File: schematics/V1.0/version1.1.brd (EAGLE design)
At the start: 66 x 45 mm, 89 parts, among them IC1 ADG1604S, IC2 LM317MBSTT3, IC3 AD8610MR, IC4 AD8610MR, IC5 337IMP, Q1 16MHz, T1 BC847, T2 BC847, T3 BC847, T4 BC847, X2 BU-SMA-H

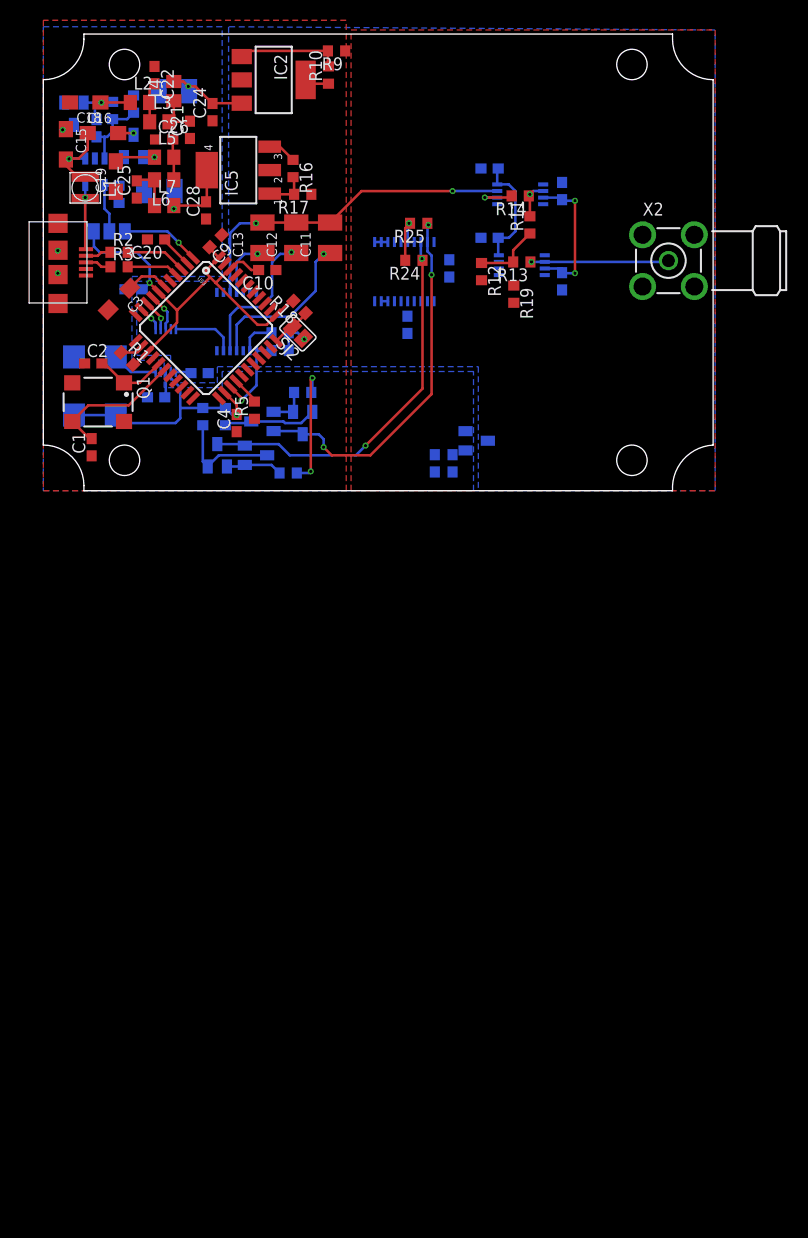
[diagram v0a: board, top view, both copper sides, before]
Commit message: change the circuit diagramm because of amplification-issues
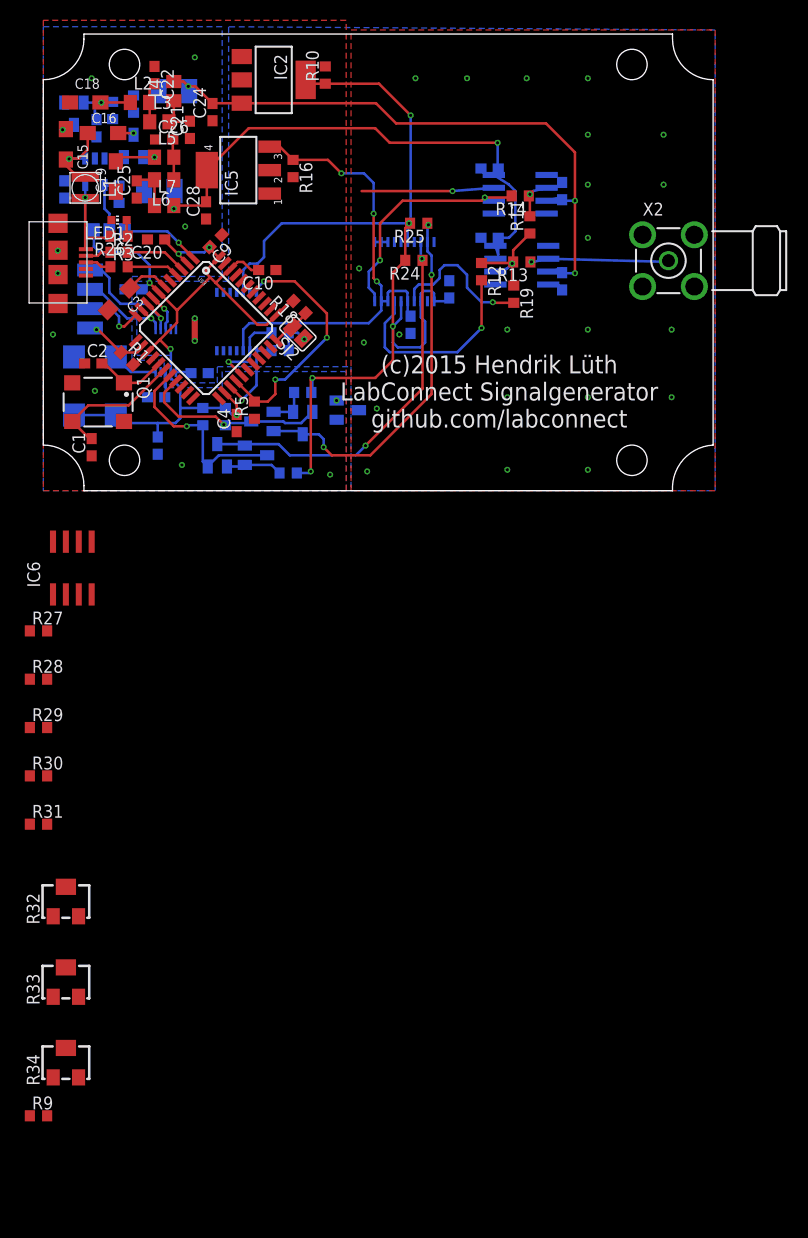
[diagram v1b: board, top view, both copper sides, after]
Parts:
- removed C11, C12, C13: (no value), rcl:SMC_B
- removed R17: 1,5k, rcl:R0603
- added IC6: AD8620R, analog-devices:SO8
- added LED1: (no value), led:CHIP-LED0603
- added PAD1, PAD2, PAD3, PAD4: (no value), wirepad:SMD1,27-2,54
- added R26: 150, rcl:R0603
- added R27, R29, R31: 10k, rcl:R0603
- added R28: 3k, rcl:R0603
- added R30: 100k, rcl:R0603
- added R32, R33: 2k, rcl:RTRIM3224W
- added R34: 100k, rcl:RTRIM3224W
- IC3, IC4: value AD8610MR -> AD8610R; device analog-devices:MSOP08 -> analog-devices:SO8
- R7: value 2M -> 1,8M
- R8: value 220k -> 100k
- R9: value 1,5k -> 10k
- moved R9 109.0 mm to (-0.48, -61.6), turned to 0 degrees
- moved C6 45.4 mm to (2.06, 29.7), turned to 270 degrees
- moved C5 29.1 mm to (11.3, 4.45)
- moved D7 13.1 mm to (30.0, 7.94)
- moved C29 2.06 mm to (40.0, 19.8)
- moved C30 0.32 mm to (36.2, 16.4)
- moved R10 0.32 mm to (27.8, 41.0)
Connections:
- new net N$50: PAD2.1, U$3.11
- new net N$51: LED1.A, R26.1
- new net N$54: R29.1, R31.2
- new net N$55: C17.1, R34.1, R7.1, U$2.3
- new net N$57: R34.2, R34.3, R9.1
- net +12V: now also IC6.8
- net -12V: now also IC6.4
- net AGND: now also IC4.3, IC6.3, IC6.5; no longer IC4.2
- net GND: now also LED1.C, R32.1, R32.2, R33.1, R33.2; no longer R17.1, R9.1
- net N$16: now also IC1.4, R28.2, R30.2; no longer IC1.6
- net N$17: now also IC6.2, R27.2, R28.1; no longer C13.+, IC1.11
- net N$18: now also IC6.1, R27.1; no longer C12.+
- net N$19: now also IC1.11, IC6.7, R31.1; no longer C11.+, IC1.4
- net N$20: now also IC1.6; no longer C11.-, C12.-, C13.-, IC1.10
- net N$27: now also R9.2; no longer C17.1, R7.1, U$2.3
- net N$30: now also R33.3; no longer R9.2
- net N$32: now also IC4.2; no longer IC4.3
- net N$4: now also PAD3.1
- net N$41: now also R32.3; no longer R17.2
- net N$53: now also IC6.6, R29.2, R30.1; no longer C20.1, U$3.2
- net N$8: now also PAD1.1
- net N$9: now also PAD4.1
- net VCC: now also C20.1, R26.2, U$3.2
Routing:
- net +3V3: track 21.1 -> 98.4 mm, vias 3 -> 5
- net -3V3: track 3.49 -> 47.2 mm, vias 0 -> 3
- net +12V: track 22.0 -> 61.0 mm
- net -12V: track 20.5 -> 54.7 mm, vias 1 -> 2
- net N$22: track 2.76 -> 24.6 mm, vias 0 -> 3
- net N$20: track 33.9 -> 13.0 mm, vias 2 -> 1
- net N$45: track 0.00 -> 20.4 mm, vias 0 -> 1
- net N$34: track 3.94 -> 23.4 mm, vias 1 -> 2
- net VCC: track 81.4 -> 97.8 mm, vias 3 -> 6
- net N$19: track 16.4 -> 0.00 mm, vias 1 -> 0
- net N$33: track 0.00 -> 14.7 mm, vias 0 -> 1
- net N$18: track 14.6 -> 0.00 mm, vias 1 -> 0
- net N$9: track 3.08 -> 12.9 mm
- net N$43: track 9.37 -> 18.9 mm, vias 0 -> 1
- net N$30: track 10.3 -> 0.87 mm
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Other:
- board text added: "(c)2015 Hendrik Lüth LabConnect Signalgenerator github.com/labconnect"

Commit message: some more changes in the circuit
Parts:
- added R17, R35: 0R, rcl:R0603
- R8: value 100k -> 150k
- R9: value 10k -> 0R
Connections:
- new net N$56: R17.1, U$1.7
- net AGND: now also R35.1
- net GND: now also R35.2
- net N$27: now also R9.1, U$1.6; no longer R8.2, R9.2
- net N$4: now also R9.2; no longer U$1.6
- net N$57: now also R8.2; no longer R9.1
- net N$9: now also R17.2; no longer U$1.7
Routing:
- net N$9: track 12.9 -> 11.8 mm
- net N$4: track 9.79 -> 9.16 mm
